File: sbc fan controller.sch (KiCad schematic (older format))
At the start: 24 parts, among them CON1 ISP-6, IC1 LM358, J1 Conn_01x13, J2 Conn_01x02, J4 Conn_01x04, J5 Conn_01x04, J6 Conn_01x03, J9 Conn_Coaxial, Q1 Q_PMOS_GSD, U1 ATTINY13A-SSU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

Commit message: Auto stash before merge of "master" and "opi_zero_fan_controller/master"
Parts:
- removed R12: 10k, Resistors_SMD:R_0805, symbol R_Small
- added J?: TEST_2P, symbol TEST_2P
- added J? (x2): TEST_1P, symbol TEST_1P
- IC1: footprint (none) -> Housings_SOIC:SOIC-8_3.9x4.9mm_Pitch1.27mm
- RN1, RN2: footprint (none) -> node_nrf:YC164J
- RV1: footprint (none) -> node_nrf:TC33
- U1: footprint Housings_SOIC:SOIC-8_3.9x4.9mm_Pitch1.27mm -> Housings_SOIC:SO-8_5.3x6.2mm_Pitch1.27mm
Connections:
- net +5V: now also RN2.1 (R1.1)
- net ADJ: now also J?.1
- net GND: now also RN2.5 (R4.2); no longer RN2.6 (R3.2)
- net ISO: now also J?.1
- net OP1_-: now also RN2.3 (R3.1); no longer RN2.2 (R2.1)
- net OP1_OUT: now also RN2.6 (R3.2); no longer RN2.8 (R1.2)
- net OP2_-: now also RN2.2 (R2.1); no longer RN2.1 (R1.1)
- net RST: now also RN2.8 (R1.2)
- net SIG+: now also RN2.4 (R4.1), J?.1; no longer RN2.3 (R3.1)
- net SIG-: no longer R7.2, TH1.1
- new net: J?.2, R7.2, TH1.1
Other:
- moved on the sheet: C1, C2, C3, C4, CON1, IC1, J1, J2, J4, J5, J6, J9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

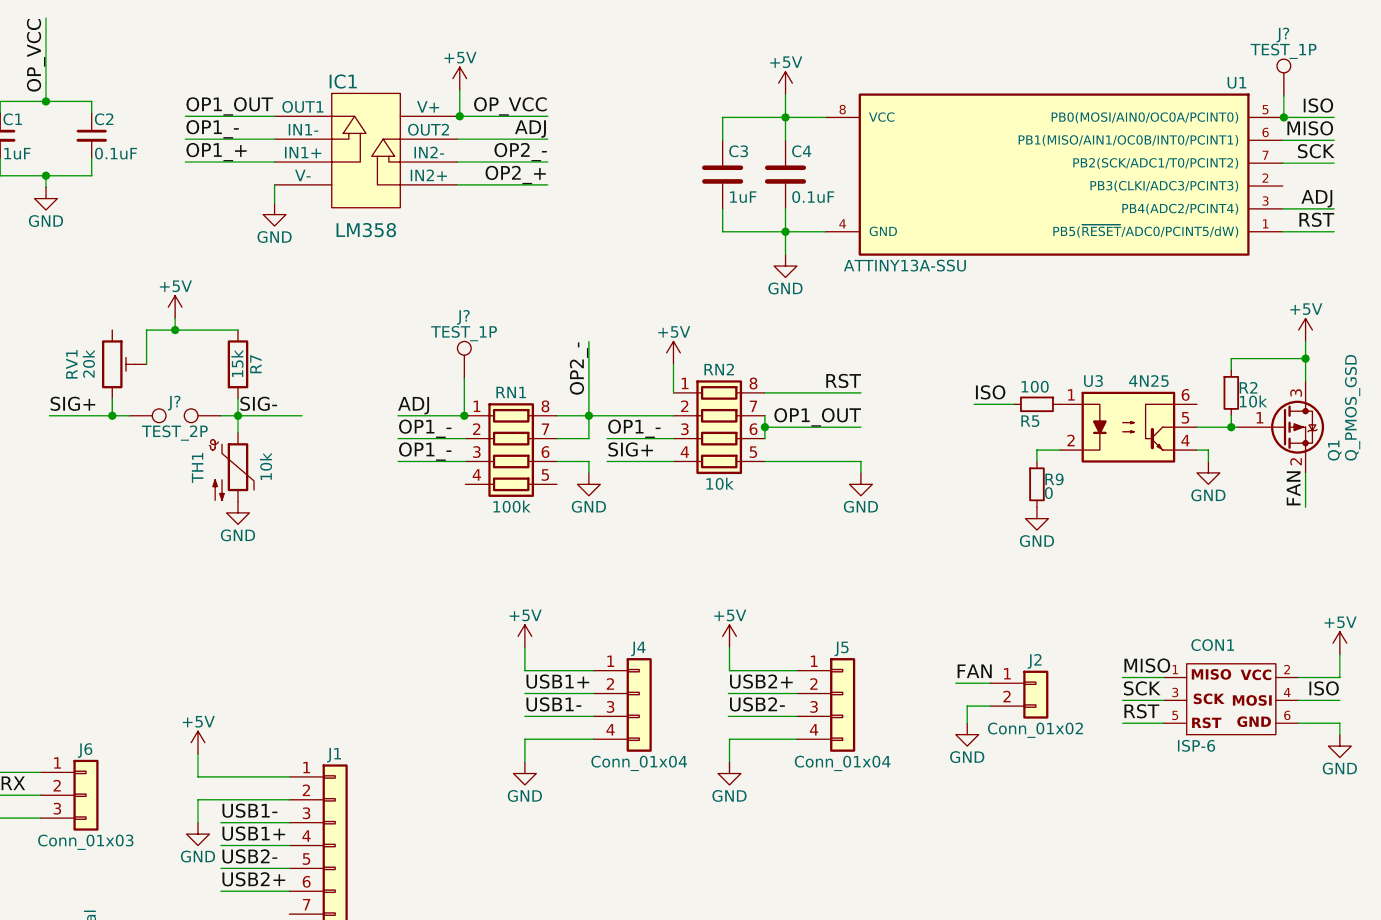
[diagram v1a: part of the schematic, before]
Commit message: Correcting references for consistency
Also added RCA coax connector, although this may not fit on the final board.
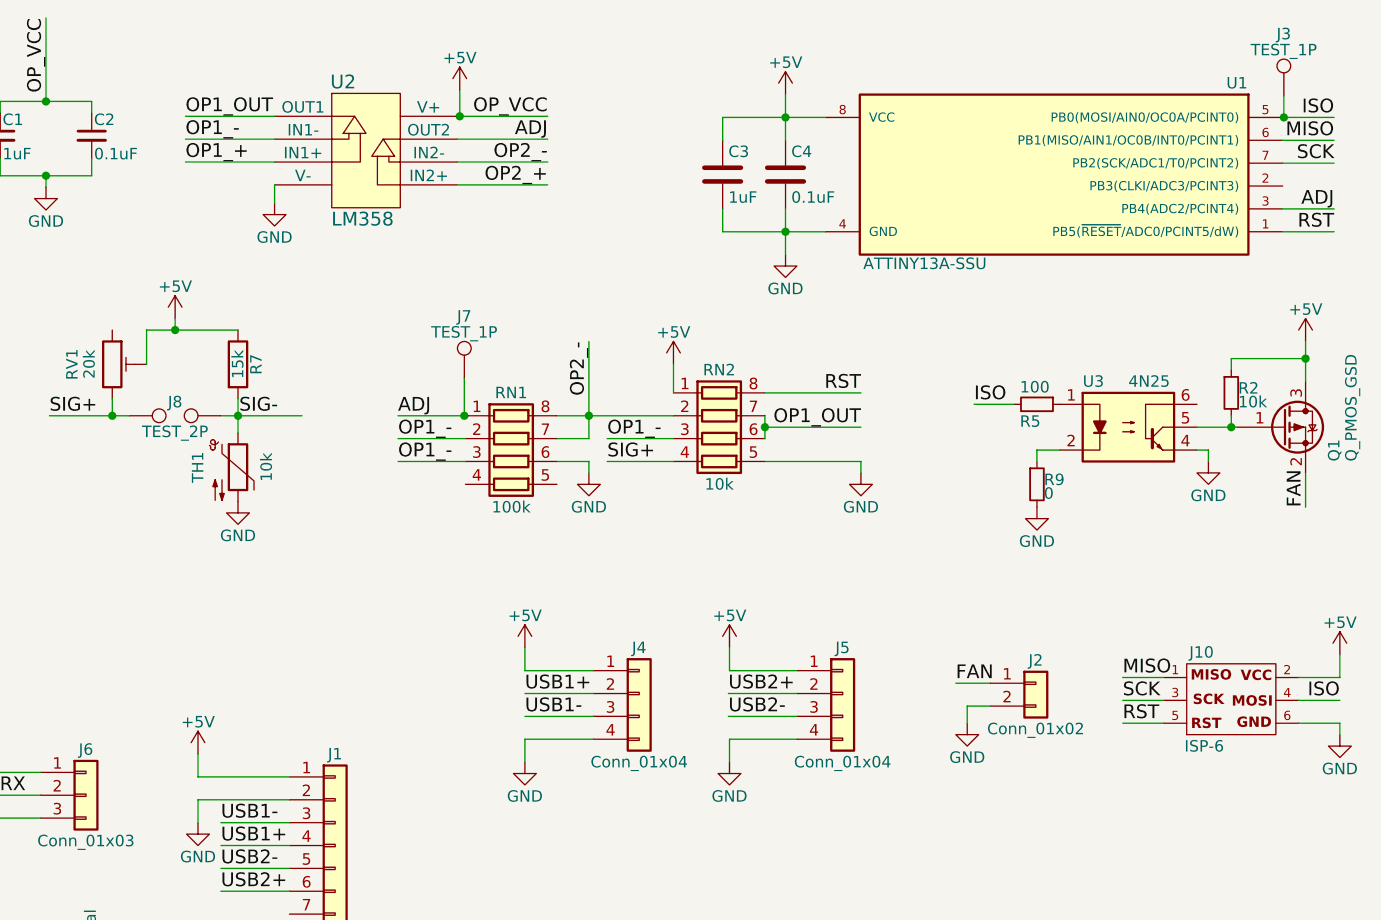
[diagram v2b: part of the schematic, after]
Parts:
- J3, J7: renamed from J?; footprint (none) -> Measurement_Points:Measurement_Point_Round-SMD-Pad_Small
- J8: renamed from J?; footprint (none) -> node_nrf:Measurement_Point_Round-SMD-2-Pad_Small
- renumbered CON1 to J10, IC1 to U2
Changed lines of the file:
@@
 P 5485 1320
 F 0 "U1" H 4685 1720 50  0000 C CNN
-F 1 "ATTINY13A-SSU" H 6135 920 50  0000 C CNN
+F 1 "ATTINY13A-SSU" H 6050 930 50  0000 C CNN
 F 2 "Housings_SOIC:SO-8_5.3x6.2mm_Pitch1.27mm" H 6085 1320 50  0001 C CIN
 F 3 "" H 4685 1670 50  0001 C CNN
@@
 $EndComp
 $Comp
-L GND #PWR01
+L GND #PWR5
 U 1 1 59C801B0
 P 4310 1670
-F 0 "#PWR01" H 4310 1420 50  0001 C CNN
+F 0 "#PWR5" H 4310 1420 50  0001 C CNN
 F 1 "GND" H 4310 1520 50  0000 C CNN
 F 2 "" H 4310 1670 50  0001 C CNN
@@
 RST
 $Comp
-L +5V #PWR02
+L +5V #PWR2
 U 1 1 59C80C50
 P 4310 970
-F 0 "#PWR02" H 4310 820 50  0001 C CNN
+F 0 "#PWR2" H 4310 820 50  0001 C CNN
 F 1 "+5V" H 4310 1110 50  0000 C CNN
 F 2 "" H 4310 970 50  0001 C CNN
@@
 $EndComp
 $Comp
-L ISP-6 CON1
+L ISP-6 J10
 U 1 1 59C806DB
 P 6285 3620
-F 0 "CON1" H 6180 3860 50  0000 C CNN
-F 1 "ISP-6" H 6020 3390 50  0000 L BNN
+F 0 "J10" H 6130 3830 50  0000 C CNN
+F 1 "ISP-6" H 6055 3390 50  0000 L BNN
 F 2 "Pin_Headers:Pin_Header_Straight_2x03_Pitch2.54mm" V 5765 3660 50  0001 C CNN
 F 3 "" H 6260 3620 50  0001 C CNN
@@
 $EndComp
 $Comp
-L GND #PWR03
+L GND #PWR18
 U 1 1 59C807F9
 P 6735 3770
-F 0 "#PWR03" H 6735 3520 50  0001 C CNN
+F 0 "#PWR18" H 6735 3520 50  0001 C CNN
 F 1 "GND" H 6735 3620 50  0000 C CNN
 F 2 "" H 6735 3770 50  0001 C CNN
@@
 $EndComp
 $Comp
-L +5V #PWR04
+L +5V #PWR16
 U 1 1 59C808AA
 P 6735 3420
-F 0 "#PWR04" H 6735 3270 50  0001 C CNN
+F 0 "#PWR16" H 6735 3270 50  0001 C CNN
 F 1 "+5V" H 6735 3560 50  0000 C CNN
 F 2 "" H 6735 3420 50  0001 C CNN
@@
 ISO
 $Comp
-L GND #PWR05
+L GND #PWR13
 U 1 1 59C81726
 P 5410 2775
-F 0 "#PWR05" H 5410 2525 50  0001 C CNN
+F 0 "#PWR13" H 5410 2525 50  0001 C CNN
 F 1 "GND" H 5410 2625 50  0000 C CNN
 F 2 "" H 5410 2775 50  0001 C CNN
@@
 $EndComp
 $Comp
-L GND #PWR06
+L GND #PWR9
 U 1 1 59C818D5
 P 6160 2575
-F 0 "#PWR06" H 6160 2325 50  0001 C CNN
+F 0 "#PWR9" H 6160 2325 50  0001 C CNN
 F 1 "GND" H 6160 2425 50  0000 C CNN
 F 2 "" H 6160 2575 50  0001 C CNN
@@
 $EndComp
 $Comp
-L +5V #PWR07
+L +5V #PWR7
 U 1 1 59C81C00
 P 6585 2050
-F 0 "#PWR07" H 6585 1900 50  0001 C CNN
+F 0 "#PWR7" H 6585 1900 50  0001 C CNN
 F 1 "+5V" H 6585 2190 50  0000 C CNN
 F 2 "" H 6585 2050 50  0001 C CNN
@@
 $EndComp
 $Comp
-L GND #PWR08
+L GND #PWR23
 U 1 1 59C93AF1
 P 1740 4155
-F 0 "#PWR08" H 1740 3905 50  0001 C CNN
+F 0 "#PWR23" H 1740 3905 50  0001 C CNN
 F 1 "GND" H 1740 4005 50  0000 C CNN
 F 2 "" H 1740 4155 50  0001 C CNN
@@
 $EndComp
 $Comp
-L GND #PWR09
+L GND #PWR17
 U 1 1 59C93BF1
 P 5105 3720
-F 0 "#PWR09" H 5105 3470 50  0001 C CNN
+F 0 "#PWR17" H 5105 3470 50  0001 C CNN
 F 1 "GND" H 5105 3570 50  0000 C CNN
 F 2 "" H 5105 3720 50  0001 C CNN
@@
 $EndComp
 $Comp
-L +5V #PWR010
+L +5V #PWR20
 U 1 1 59C93CE3
 P 1740 3855
-F 0 "#PWR010" H 1740 3705 50  0001 C CNN
+F 0 "#PWR20" H 1740 3705 50  0001 C CNN
 F 1 "+5V" H 1740 3995 50  0000 C CNN
 F 2 "" H 1740 3855 50  0001 C CNN
@@
 $EndComp
 $Comp
-L +5V #PWR011
+L +5V #PWR6
 U 1 1 5A2BCFF8
 P 1640 1950
-F 0 "#PWR011" H 1640 1800 50  0001 C CNN
+F 0 "#PWR6" H 1640 1800 50  0001 C CNN
 F 1 "+5V" H 1640 2090 50  0000 C CNN
 F 2 "" H 1640 1950 50  0001 C CNN
@@
 $EndComp
 $Comp
-L GND #PWR012
+L GND #PWR12
 U 1 1 5A2BD03E
 P 1915 2750
-F 0 "#PWR012" H 1915 2500 50  0001 C CNN
+F 0 "#PWR12" H 1915 2500 50  0001 C CNN
 F 1 "GND" H 1915 2600 50  0000 C CNN
 F 2 "" H 1915 2750 50  0001 C CNN
@@
 $EndComp
 $Comp
-L +5V #PWR013
+L +5V #PWR15
 U 1 1 5A2C324E
 P 4065 3390
-F 0 "#PWR013" H 4065 3240 50  0001 C CNN
+F 0 "#PWR15" H 4065 3240 50  0001 C CNN
 F 1 "+5V" H 4065 3530 50  0000 C CNN
 F 2 "" H 4065 3390 50  0001 C CNN
@@
 $EndComp
 $Comp
-L GND #PWR014
+L GND #PWR22
 U 1 1 5A2C33FF
 P 4065 3890
-F 0 "#PWR014" H 4065 3640 50  0001 C CNN
+F 0 "#PWR22" H 4065 3640 50  0001 C CNN
 F 1 "GND" H 4065 3740 50  0000 C CNN
 F 2 "" H 4065 3890 50  0001 C CNN
@@
 $EndComp
 $Comp
-L +5V #PWR015
+L +5V #PWR14
 U 1 1 5A2C3DEC
 P 3170 3390
-F 0 "#PWR015" H 3170 3240 50  0001 C CNN
+F 0 "#PWR14" H 3170 3240 50  0001 C CNN
 F 1 "+5V" H 3170 3530 50  0000 C CNN
 F 2 "" H 3170 3390 50  0001 C CNN
@@
 $EndComp
 $Comp
-L GND #PWR016
+L GND #PWR21
 U 1 1 5A2C3DF6
 P 3170 3890
-F 0 "#PWR016" H 3170 3640 50  0001 C CNN
+F 0 "#PWR21" H 3170 3640 50  0001 C CNN
 F 1 "GND" H 3170 3740 50  0000 C CNN
 F 2 "" H 3170 3890 50  0001 C CNN
@@
 $EndComp
 $Comp
-L GND #PWR017
+L GND #PWR25
 U 1 1 5A2CA05F
 P 1155 4965
-F 0 "#PWR017" H 1155 4715 50  0001 C CNN
+F 0 "#PWR25" H 1155 4715 50  0001 C CNN
 F 1 "GND" H 1155 4815 50  0000 C CNN
 F 2 "" H 1155 4965 50  0001 C CNN
@@
 $EndComp
 $Comp
-L GND #PWR018
+L GND #PWR3
 U 1 1 5A2CF5BB
 P 1075 1375
-F 0 "#PWR018" H 1075 1125 50  0001 C CNN
+F 0 "#PWR3" H 1075 1125 50  0001 C CNN
 F 1 "GND" H 1075 1225 50  0000 C CNN
 F 2 "" H 1075 1375 50  0001 C CNN
@@
 $EndComp
 $Comp
-L TL972 IC1
+L TL972 U2
 U 1 1 5A31BEE4
 P 2475 1215
-F 0 "IC1" H 2375 1515 60  0000 C CNN
-F 1 "LM358" H 2475 865 60  0000 C CNN
+F 0 "U2" H 2375 1515 60  0000 C CNN
+F 1 "LM358" H 2460 915 60  0000 C CNN
 F 2 "Housings_SOIC:SOIC-8_3.9x4.9mm_Pitch1.27mm" H 2525 1215 60  0001 C CNN
 F 3 "" H 2525 1215 60  0001 C CNN
@@
 OP2_+
 $Comp
-L GND #PWR019
+L GND #PWR4
 U 1 1 5A31D9E1
 P 2075 1445
-F 0 "#PWR019" H 2075 1195 50  0001 C CNN
+F 0 "#PWR4" H 2075 1195 50  0001 C CNN
 F 1 "GND" H 2075 1295 50  0000 C CNN
 F 2 "" H 2075 1445 50  0001 C CNN
@@
 $EndComp
 $Comp
-L +5V #PWR020
+L +5V #PWR1
 U 1 1 5A31E249
 P 2885 950
-F 0 "#PWR020" H 2885 800 50  0001 C CNN
+F 0 "#PWR1" H 2885 800 50  0001 C CNN
 F 1 "+5V" H 2885 1090 50  0000 C CNN
 F 2 "" H 2885 950 50  0001 C CNN
@@
 $EndComp
 $Comp
-L GND #PWR021
+L GND #PWR11
 U 1 1 5A33257A
 P 4640 2625
-F 0 "#PWR021" H 4640 2375 50  0001 C CNN
+F 0 "#PWR11" H 4640 2375 50  0001 C CNN
 F 1 "GND" H 4640 2475 50  0000 C CNN
 F 2 "" H 4640 2625 50  0001 C CNN
@@
 $EndComp
 $Comp
-L GND #PWR022
+L GND #PWR10
 U 1 1 5A332679
 P 3450 2625
-F 0 "#PWR022" H 3450 2375 50  0001 C CNN
+F 0 "#PWR10" H 3450 2375 50  0001 C CNN
 F 1 "GND" H 3450 2475 50  0000 C CNN
 F 2 "" H 3450 2625 50  0001 C CNN
@@
 IR_RX
 $Comp
-L +5V #PWR023
+L +5V #PWR19
 U 1 1 5A2C987B
 P 750 3810
-F 0 "#PWR023" H 750 3660 50  0001 C CNN
+F 0 "#PWR19" H 750 3660 50  0001 C CNN
 F 1 "+5V" H 750 3950 50  0000 C CNN
 F 2 "" H 750 3810 50  0001 C CNN
@@
 IR_RX
 $Comp
-L GND #PWR024
+L GND #PWR24
 U 1 1 5A2C7945
 P 750 4235
-F 0 "#PWR024" H 750 3985 50  0001 C CNN
+F 0 "#PWR24" H 750 3985 50  0001 C CNN
 F 1 "GND" H 750 4085 50  0000 C CNN
 F 2 "" H 750 4235 50  0001 C CNN
@@
 RST
 $Comp
-L +5V #PWR025
+L +5V #PWR8
 U 1 1 5A33F393
 P 3820 2150
-F 0 "#PWR025" H 3820 2000 50  0001 C CNN
+F 0 "#PWR8" H 3820 2000 50  0001 C CNN
 F 1 "+5V" H 3820 2290 50  0000 C CNN
 F 2 "" H 3820 2150 50  0001 C CNN
@@
 $EndComp
 $Comp
-L TEST_2P J?
+L TEST_2P J8
 U 1 1 5A340887
 P 1640 2375
-F 0 "J?" H 1640 2435 50  0000 C CNN
+F 0 "J8" H 1640 2435 50  0000 C CNN
 F 1 "TEST_2P" H 1640 2305 50  0000 C CNN
-F 2 "" H 1640 2375 50  0001 C CNN
+F 2 "node_nrf:Measurement_Point_Round-SMD-2-Pad_Small" H 1640 2375 50  0001 C CNN
 F 3 "" H 1640 2375 50  0001 C CNN
 	1    1640 2375
@@
 $EndComp
 $Comp
-L TEST_1P J?
+L TEST_1P J7
 U 1 1 5A3418D8
 P 2905 2210
-F 0 "J?" H 2905 2480 50  0000 C CNN
+F 0 "J7" H 2905 2480 50  0000 C CNN
 F 1 "TEST_1P" H 2905 2410 50  0000 C CNN
-F 2 "" H 3105 2210 50  0001 C CNN
+F 2 "Measurement_Points:Measurement_Point_Round-SMD-Pad_Small" H 3105 2210 50  0001 C CNN
 F 3 "" H 3105 2210 50  0001 C CNN
 	1    2905 2210
@@
 Connection ~ 2905 2375
 $Comp
-L TEST_1P J?
+L TEST_1P J3
 U 1 1 5A342349
 P 6490 975
-F 0 "J?" H 6490 1245 50  0000 C CNN
+F 0 "J3" H 6490 1245 50  0000 C CNN
 F 1 "TEST_1P" H 6490 1175 50  0000 C CNN
-F 2 "" H 6690 975 50  0001 C CNN
+F 2 "Measurement_Points:Measurement_Point_Round-SMD-Pad_Small" H 6690 975 50  0001 C CNN
 F 3 "" H 6690 975 50  0001 C CNN
 	1    6490 975

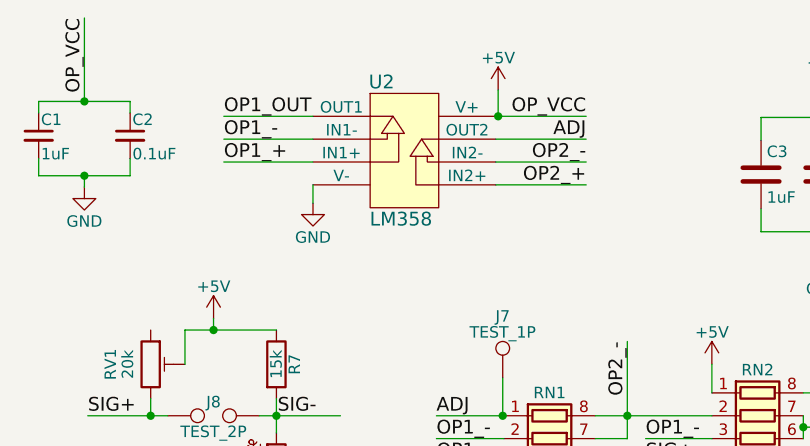
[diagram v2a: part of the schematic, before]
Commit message: Corrected non-inverting signal input network names
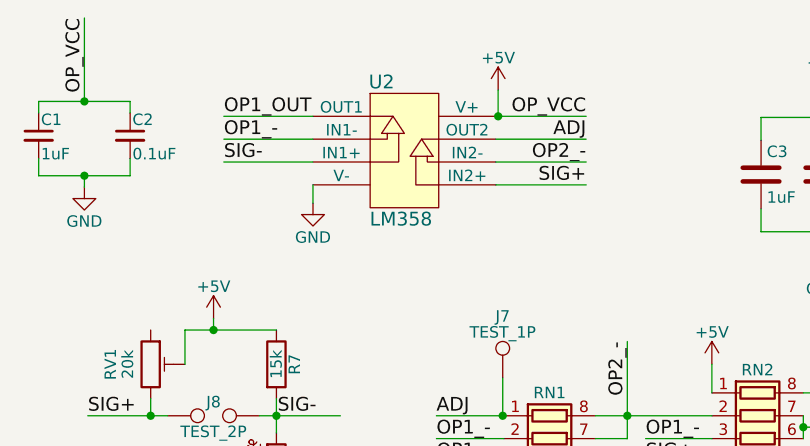
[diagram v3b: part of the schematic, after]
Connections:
- net OP1_+ is gone; now on net SIG-: U2.3 (IN1+)
- net OP2_+ is gone; now on net SIG+: U2.5 (IN2+)
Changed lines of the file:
@@
 $EndComp
 Text Label 3270 1365 2    60   ~ 0
-OP2_+
+SIG+
 $Comp
 L GND #PWR4
@@
 $EndComp
 Text Label 1685 1265 0    60   ~ 0
-OP1_+
+SIG-
 Text Label 3270 1265 2    60   ~ 0
 OP2_-

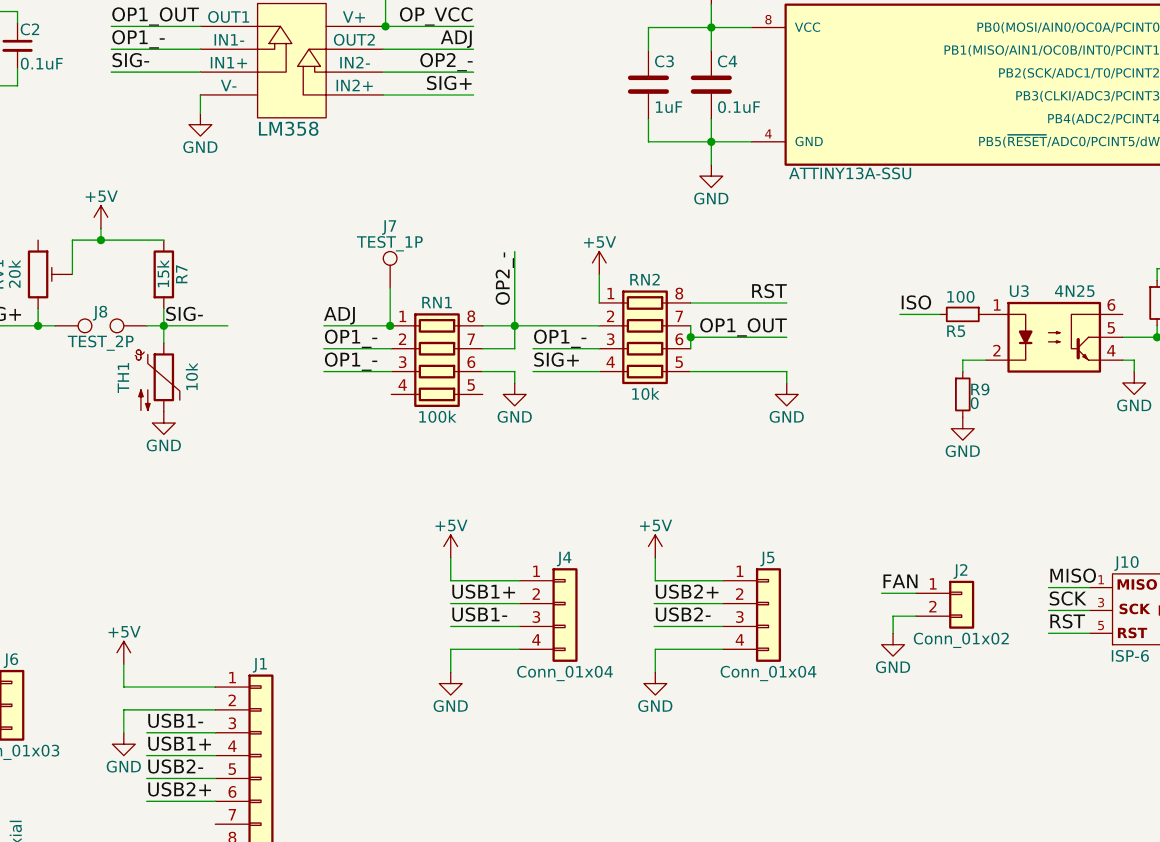
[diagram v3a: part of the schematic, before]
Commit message: Minor layout corrections
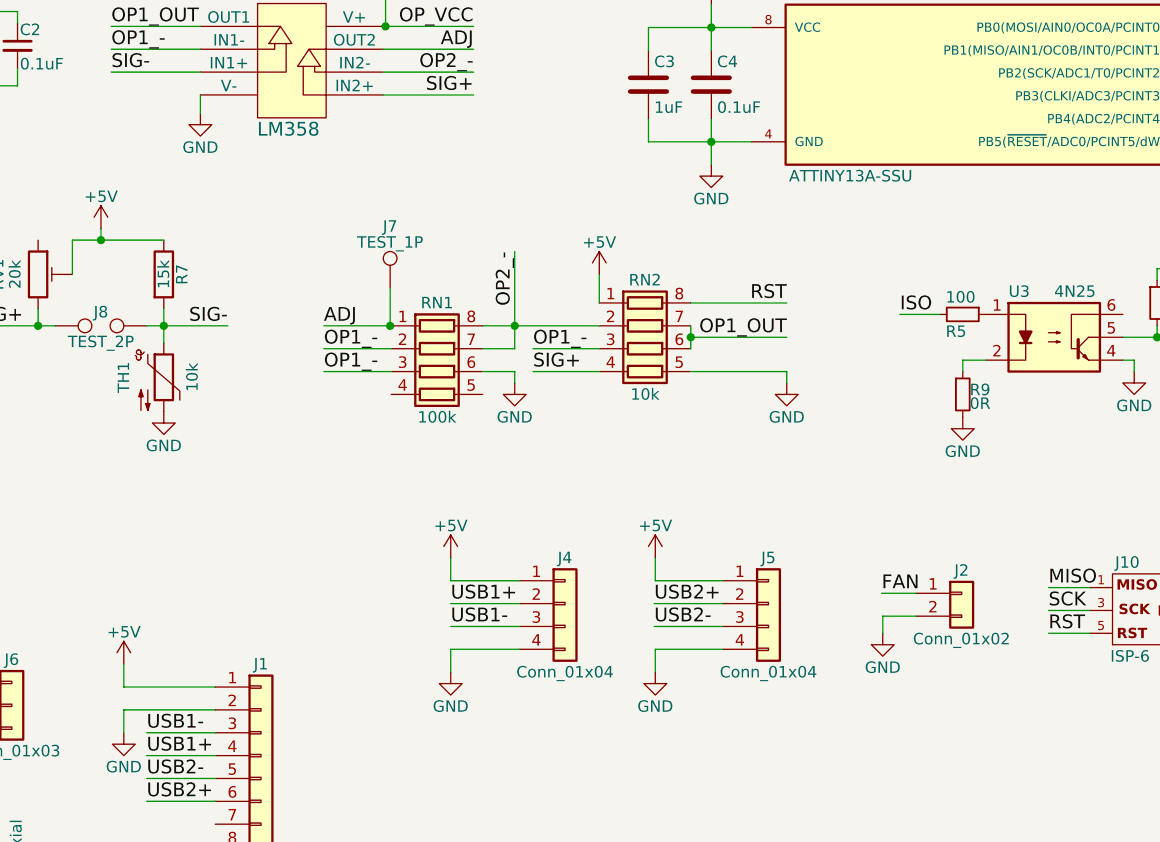
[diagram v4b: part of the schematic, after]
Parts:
- R9: value 0 -> 0R
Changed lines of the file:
@@
 P 5485 1320
 F 0 "U1" H 4685 1720 50  0000 C CNN
-F 1 "ATTINY13A-SSU" H 6050 930 50  0000 C CNN
+F 1 "ATTINY13A-SSU" H 6050 920 50  0000 C CNN
 F 2 "Housings_SOIC:SO-8_5.3x6.2mm_Pitch1.27mm" H 6085 1320 50  0001 C CIN
 F 3 "" H 4685 1670 50  0001 C CNN
@@
 P 5410 2675
 F 0 "R9" H 5440 2695 50  0000 L CNN
-F 1 "0" H 5440 2635 50  0000 L CNN
+F 1 "0R" H 5440 2635 50  0000 L CNN
 F 2 "Resistors_SMD:R_0805" H 5410 2675 50  0001 C CNN
 F 3 "" H 5410 2675 50  0001 C CNN
@@
 L GND #PWR17
 U 1 1 59C93BF1
-P 5105 3720
-F 0 "#PWR17" H 5105 3470 50  0001 C CNN
-F 1 "GND" H 5105 3570 50  0000 C CNN
-F 2 "" H 5105 3720 50  0001 C CNN
-F 3 "" H 5105 3720 50  0001 C CNN
-	1    5105 3720
+P 5060 3720
+F 0 "#PWR17" H 5060 3470 50  0001 C CNN
+F 1 "GND" H 5060 3570 50  0000 C CNN
+F 2 "" H 5060 3720 50  0001 C CNN
+F 3 "" H 5060 3720 50  0001 C CNN
+	1    5060 3720
 	1    0    0    -1
 $EndComp
@@
 	1    0    0    -1
 $EndComp
-Text Label 1920 2375 0    60   ~ 0
+Text Label 2195 2375 2    60   ~ 0
 SIG-
 Text Label 1090 2375 0    60   ~ 0
@@
 	1740 4055 2140 4055
 Wire Wire Line
-	5205 3645 5105 3645
-Wire Wire Line
-	5105 3645 5105 3720
+	5060 3645 5205 3645
+Wire Wire Line
+	5060 3645 5060 3720
 Wire Wire Line
 	1740 3955 2140 3955
